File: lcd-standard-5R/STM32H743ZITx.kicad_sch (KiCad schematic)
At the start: 37 parts, among them J2 SWD, J3 Conn_ARM_JTAG_SWD_10, SW1 SW_Push, SW2 SW_Push, U10 STM32H743ZITx, Y1 25MHz, Y2 32.768KHz

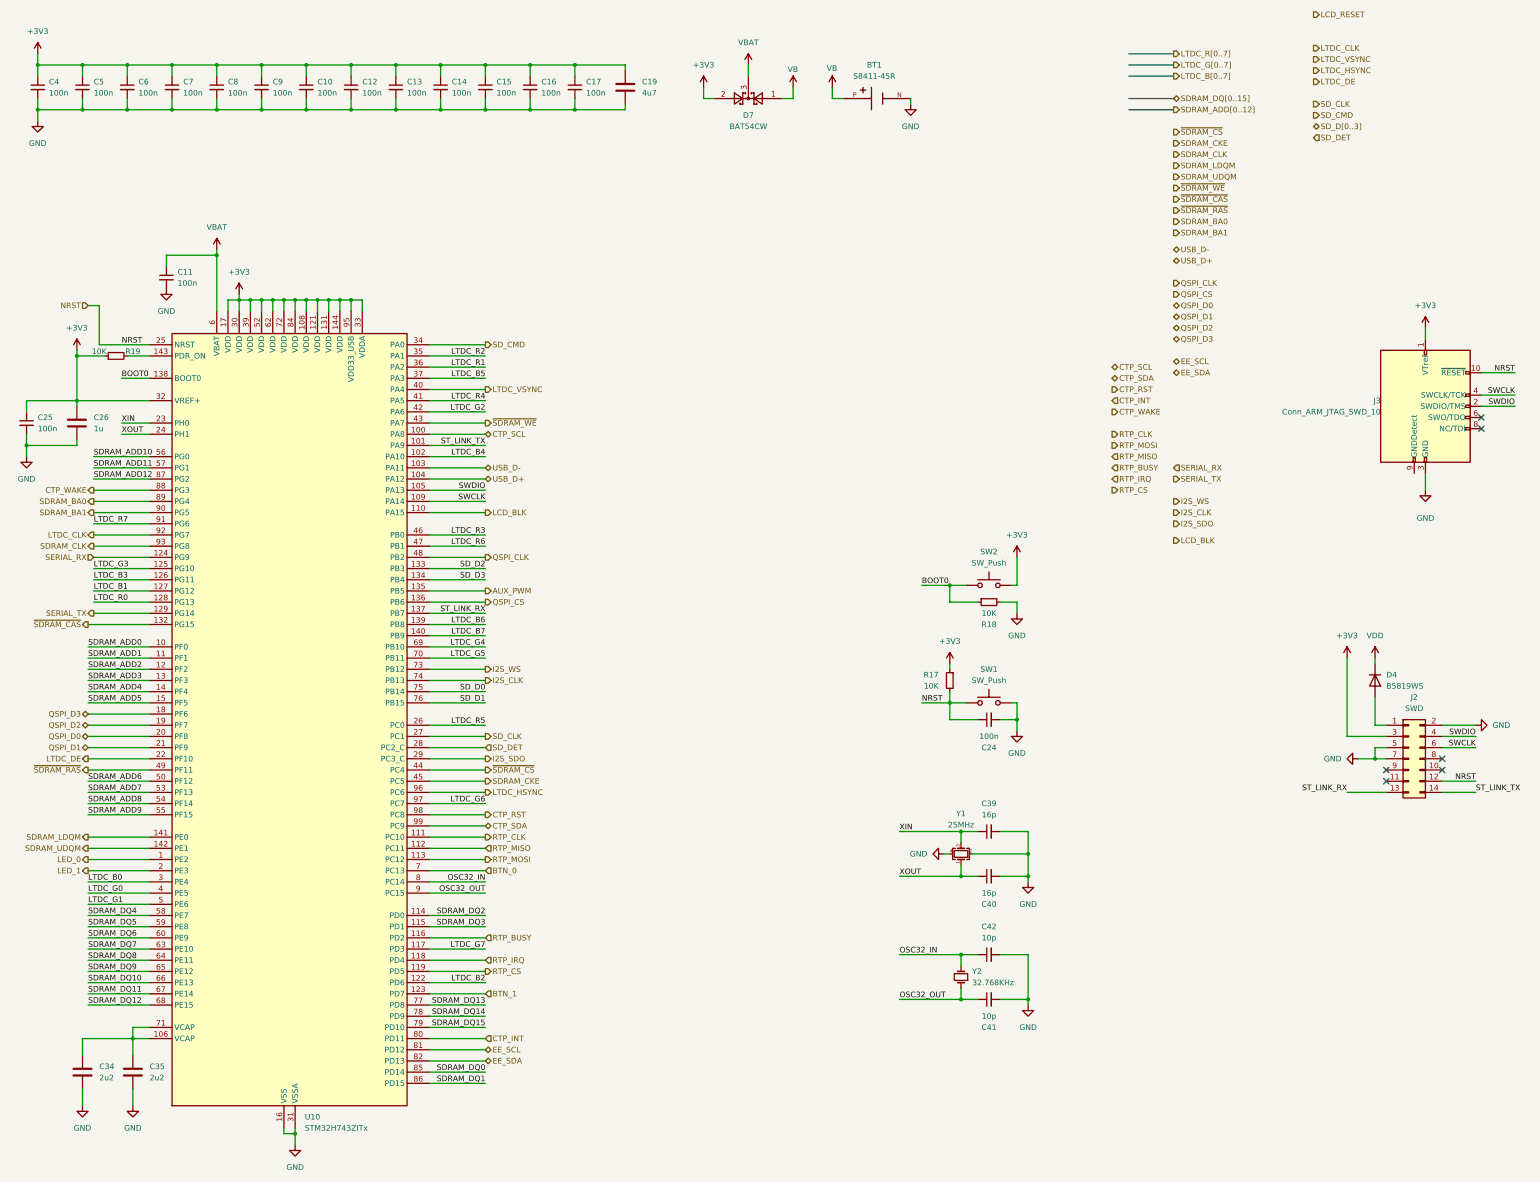
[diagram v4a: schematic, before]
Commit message: Add QSPI Flash trace length matching to 5 inch LCD
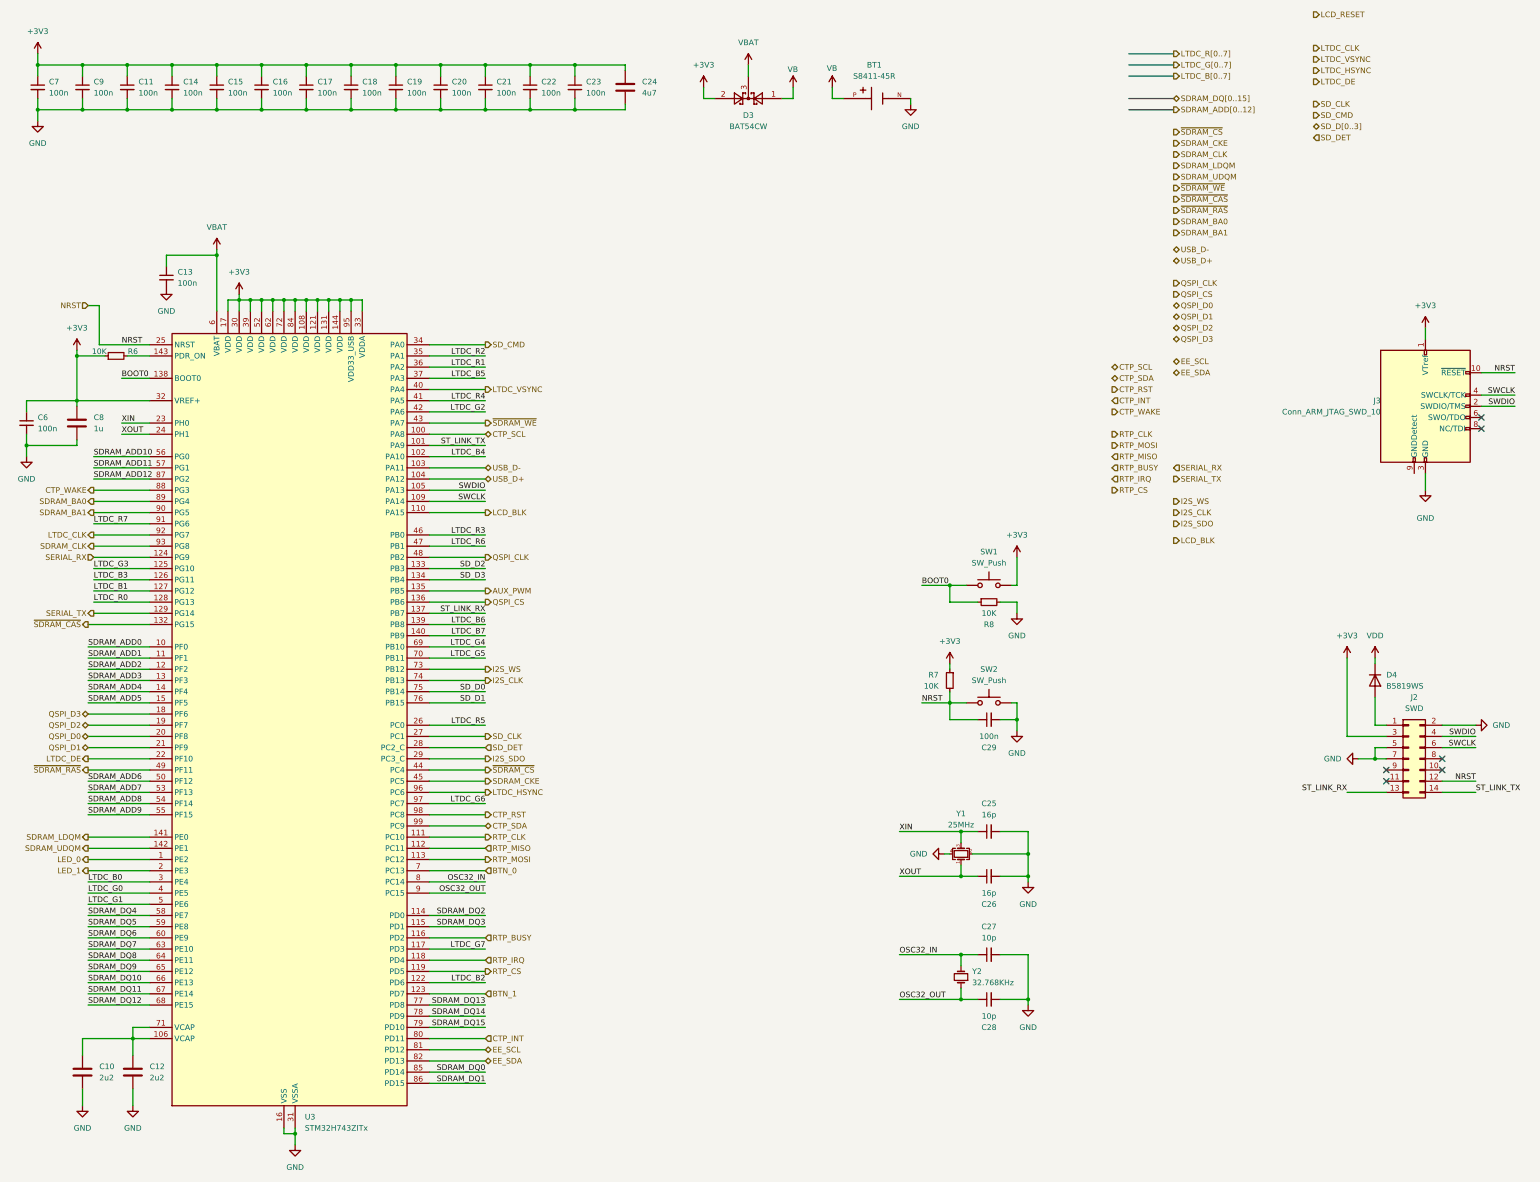
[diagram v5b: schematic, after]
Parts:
- renumbered C34 to C10, C6 to C11, C35 to C12, C11 to C13, C7 to C14, C8 to C15, C9 to C16, C10 to C17, C12 to C18, C13 to C19, C14 to C20, C15 to C21, C16 to C22, C17 to C23, C19 to C24, C39 to C25, C40 to C26, C42 to C27, C41 to C28, C24 to C29, C25 to C6, C4 to C7, C26 to C8, C5 to C9, D7 to D3, R19 to R6, R17 to R7, R18 to R8, SW2 to SW1, SW1 to SW2, U10 to U3

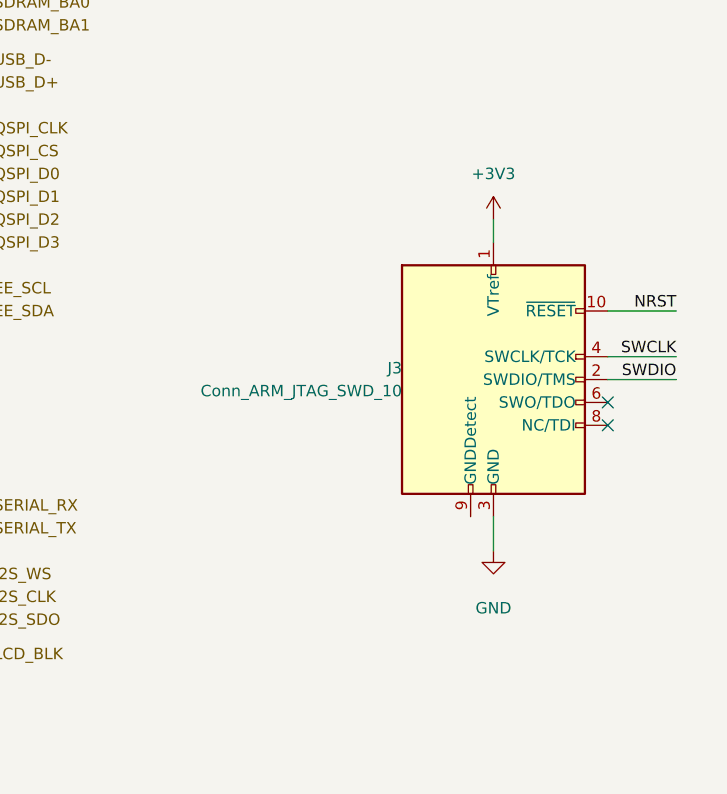
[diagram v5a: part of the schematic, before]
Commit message: Change standoff dimension to match TJC LCD
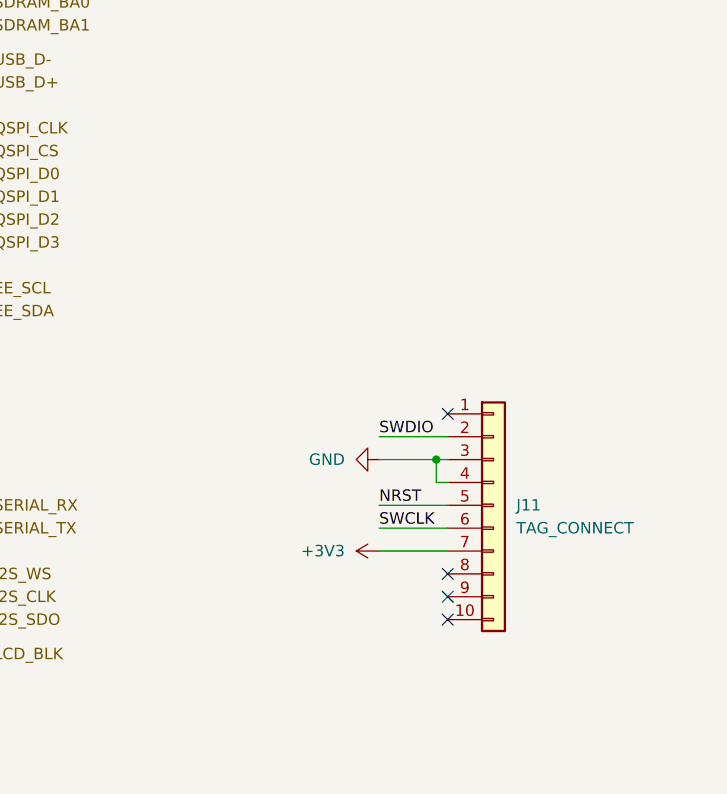
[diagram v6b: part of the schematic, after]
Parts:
- removed J3: Conn_ARM_JTAG_SWD_10, Connector:Tag-Connect_TC2050-IDC-NL_2x05_P1.27mm_Vertical, symbol Connector:Conn_ARM_JTAG_SWD_10
- added J11: TAG_CONNECT, Connector:Tag-Connect_TC2050-IDC-NL_2x05_P1.27mm_Vertical, symbol Connector_Generic:Conn_01x10
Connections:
- net +3V3: now also J11.7 (Pin_7)
- net GND: now also J11.3 (Pin_3), J11.4 (Pin_4)
- net NRST: now also J11.5 (Pin_5)
- net SWCLK: now also J11.6 (Pin_6)
- net SWDIO: now also J11.2 (Pin_2)
- no-connect marks 6 -> 8
